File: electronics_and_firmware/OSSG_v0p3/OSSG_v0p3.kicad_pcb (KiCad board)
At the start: 4 copper layers, 85 x 9 mm, 64 parts, among them IC1 DW01A, J1 USB_B_Micro, Q1 FS8205A, Q2 Q_NPN_BEC, Q3 Q_NPN_BEC, SW1 SW_SPST, U1 ESP32-PICO-D4, U2 TP4056, U3 XC6222B331MRG, U4 FT232RQ

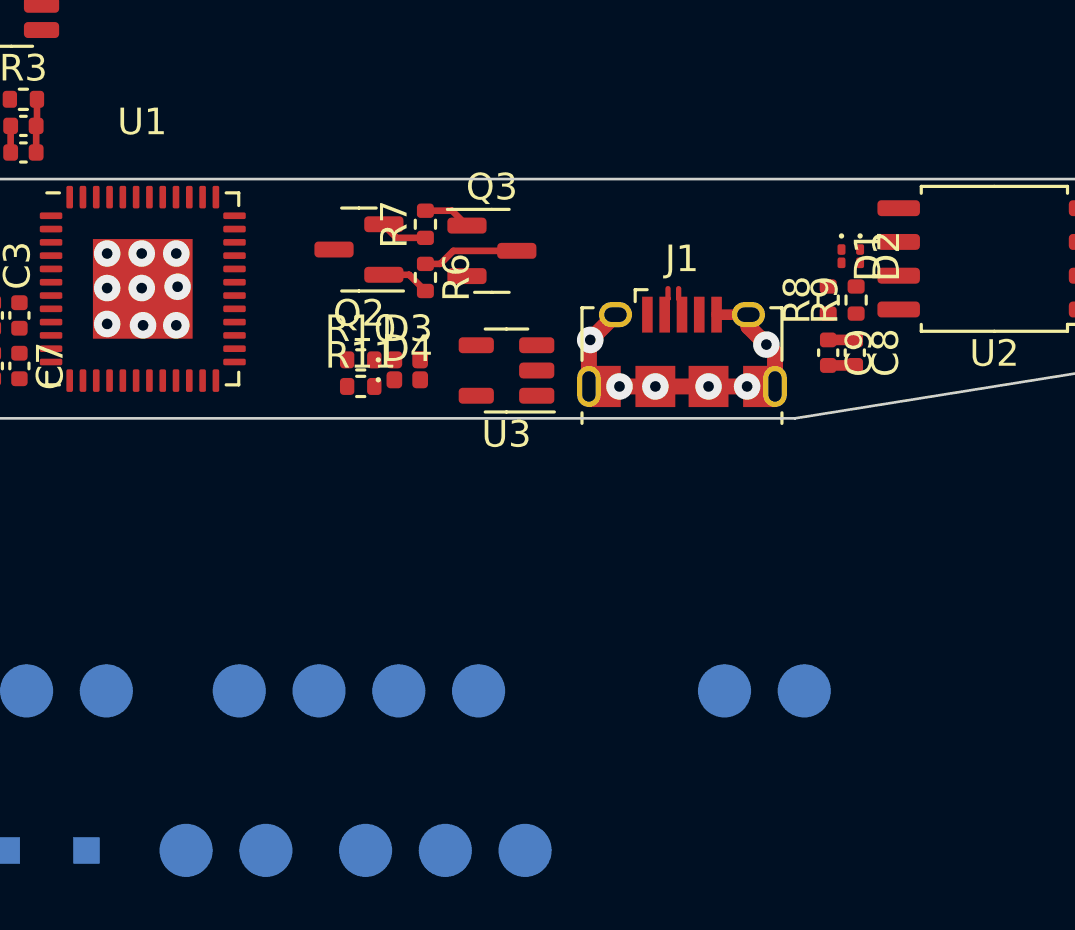
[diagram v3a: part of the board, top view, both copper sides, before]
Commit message: fix TX/RX switch, fix DW01A transistor symbol, update footprint sizes, remove IO0 and GPIOs at north side of ESP32-PICO-D4
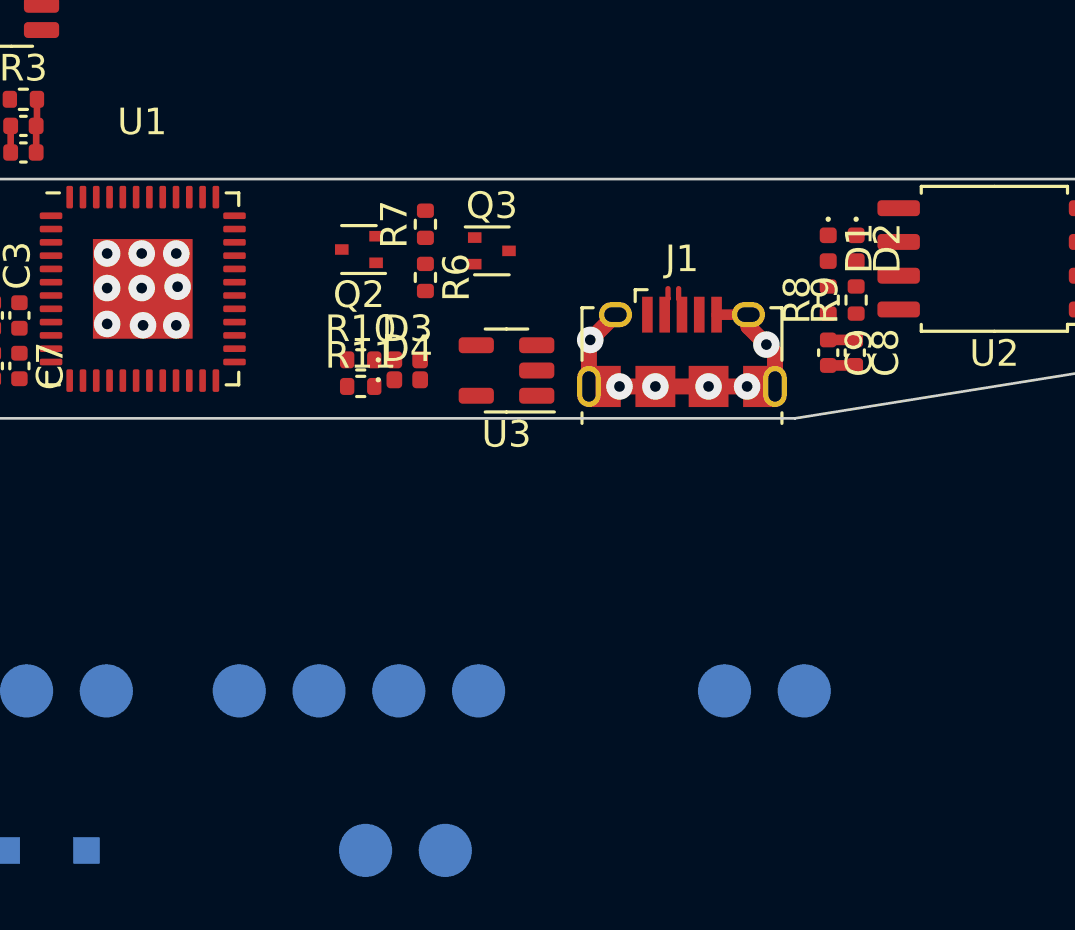
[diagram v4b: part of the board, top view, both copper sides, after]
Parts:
- removed TP23: IO0_Breakout, OpenSourceSmartGlasses:BreakoutPadSmall
- removed TP8: IO21_I2C_SDA0, OpenSourceSmartGlasses:BreakoutPadSmall
- removed TP9: IO22_I2C_SCL0, OpenSourceSmartGlasses:BreakoutPadSmall
- D1, D2: footprint Diode_SMD:D_01005_0402Metric -> Diode_SMD:D_0402_1005Metric
- Q2, Q3: footprint Package_TO_SOT_SMD:SOT-23 -> Package_TO_SOT_SMD:SOT-523
- moved D1 0.58 mm to (136.2, 77.6)
- moved D2 0.34 mm to (137.3, 77.6)
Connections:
- Q1 pad 1: Net-(Q1-Pad1) -> GND
- Q1 pad 2: BATT- -> unconnected-(Q1-Pad2)
- Q1 pad 5: Net-(IC1-Pad3) -> unconnected-(Q1-Pad5)
- Q1 pad 6: GND -> Net-(IC1-Pad3)
- TP3 pad 1: RXD -> TX_ESP
- TP4 pad 1: TXD -> RX_ESP
- U1 pad 40: RXD -> RX_ESP
- U1 pad 41: TXD -> TX_ESP
- U4 pad 2: RXD -> TX_ESP
- U4 pad 30: TXD -> RX_ESP
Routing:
- net DTR: track 3.64 -> 0.00 mm
- net Net-(Q2-Pad1): track 1.82 -> 0.00 mm
- net RTS: track 1.80 -> 0.00 mm
- net Net-(Q3-Pad1): track 1.79 -> 0.00 mm

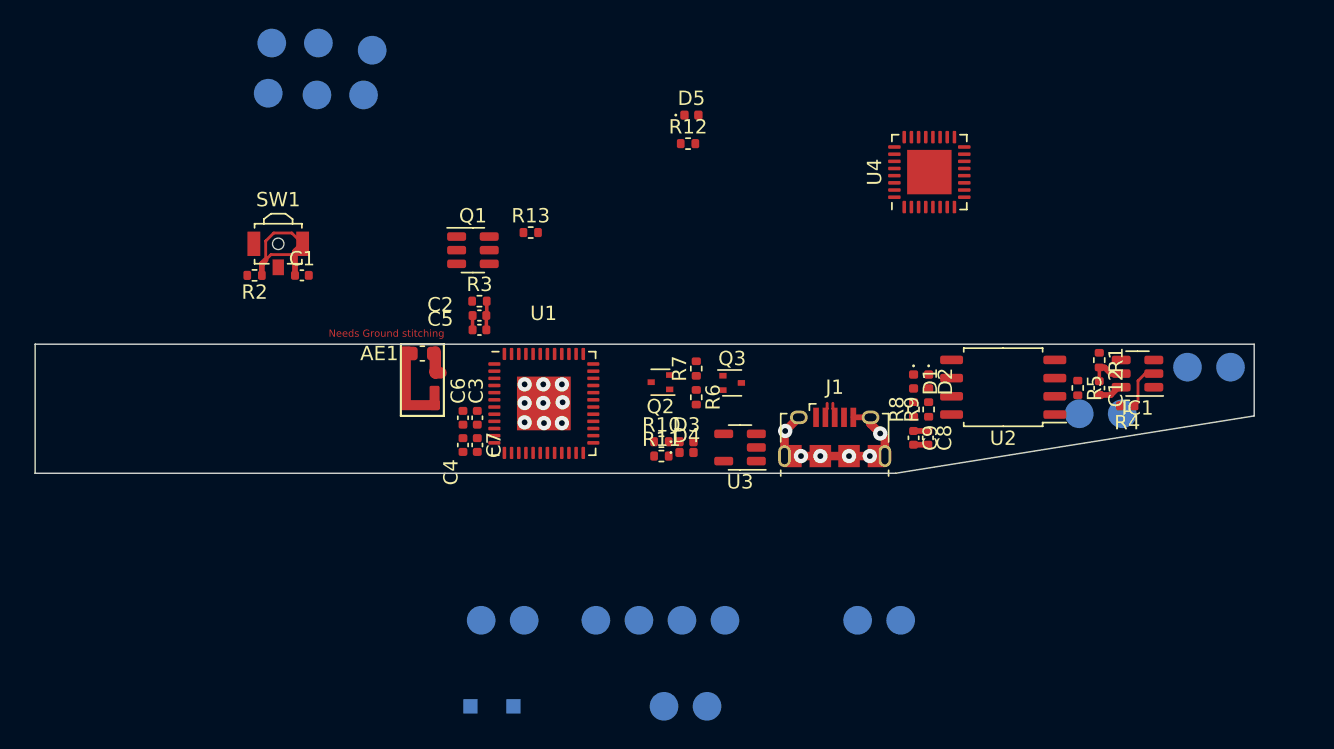
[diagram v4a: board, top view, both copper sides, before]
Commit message: more work on layout, small schematic fixes
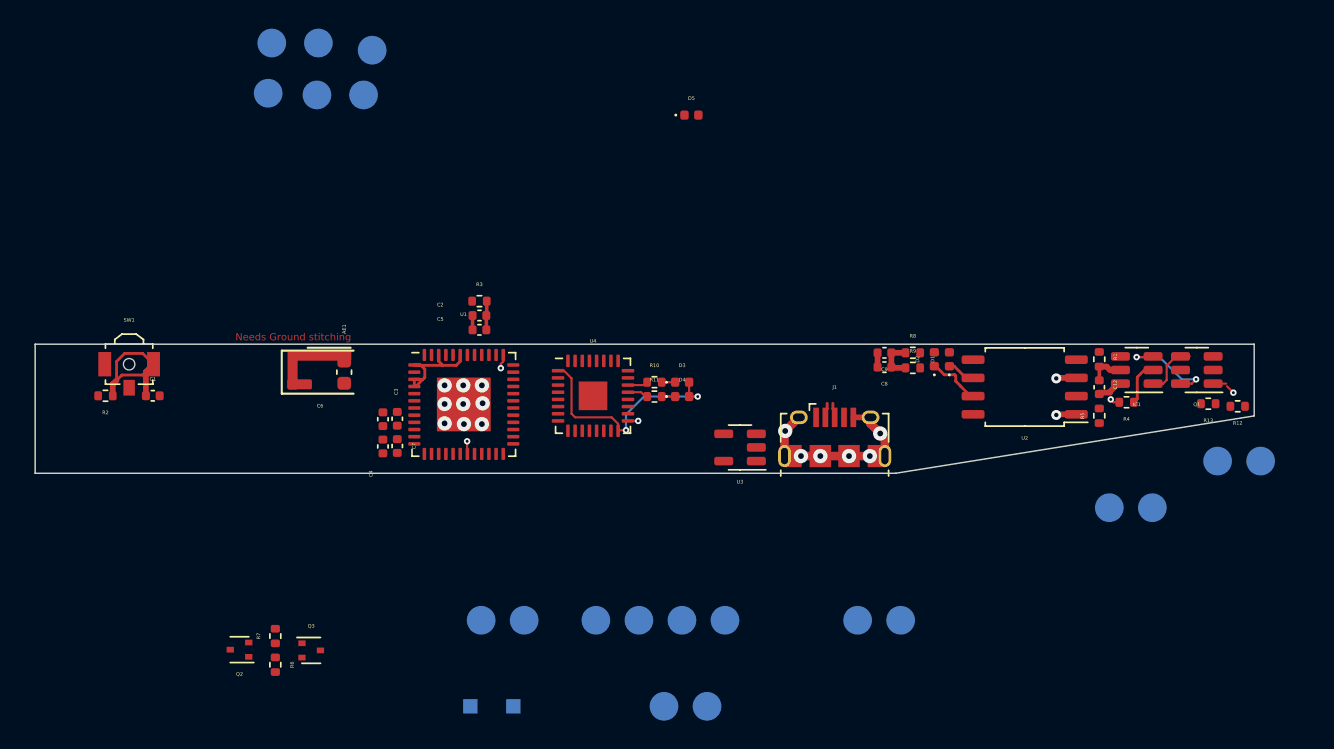
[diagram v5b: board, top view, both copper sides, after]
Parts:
- moved Q1 51.2 mm to (156.0, 76.8), turned to 180 degrees
- moved R13 48.7 mm to (156.8, 79.2), turned to 180 degrees
- moved R12 42.5 mm to (158.8, 79.3), turned to 180 degrees
- moved Q2 34.8 mm to (89.2, 96.3)
- moved Q3 34.8 mm to (94.2, 96.3)
- moved R6 34.8 mm to (91.8, 97.3)
- moved R7 34.8 mm to (91.8, 95.3)
- moved U4 28.2 mm to (113.9, 78.6), turned to 0 degrees
- moved SW1 13.4 mm to (81.6, 77.2)
- moved C1 13.4 mm to (83.2, 78.6)
- moved R2 13.4 mm to (79.9, 78.6)
- moved TP13 6.88 mm to (157.4, 83.2)
- moved TP14 6.88 mm to (149.9, 86.4)
- moved TP15 6.88 mm to (160.4, 83.2)
- moved TP16 6.88 mm to (152.9, 86.4)
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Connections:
- U1 pad 19: +3.3VA -> +3V3
- U1 pad 37: +3.3VA -> +3V3
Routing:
- net VCCIO: track 0.00 -> 16.4 mm, vias 0 -> 2
- net +3.3VA: track 2.01 -> 10.1 mm
- net Net-(IC1-Pad3): track 0.00 -> 7.17 mm, vias 0 -> 2
- net GND: track 15.5 -> 20.6 mm, vias 15 -> 20
- net Net-(D2-Pad1): track 0.00 -> 3.79 mm
- net Net-(IC1-Pad1): track 0.00 -> 3.60 mm
- net VCC_IN: track 1.06 -> 3.06 mm
- net Net-(D1-Pad1): track 0.00 -> 1.99 mm
- net +3V3: track 0.00 -> 1.88 mm, vias 0 -> 2
- net Net-(AE1-Pad1): track 1.86 -> 0.00 mm
- net Net-(R11-Pad1): track 0.00 -> 1.46 mm
- net Net-(R10-Pad1): track 0.00 -> 1.42 mm
- net Net-(D4-Pad1): track 0.00 -> 0.94 mm
- net Net-(D3-Pad1): track 0.00 -> 0.94 mm

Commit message: Changed antenna and routing progress
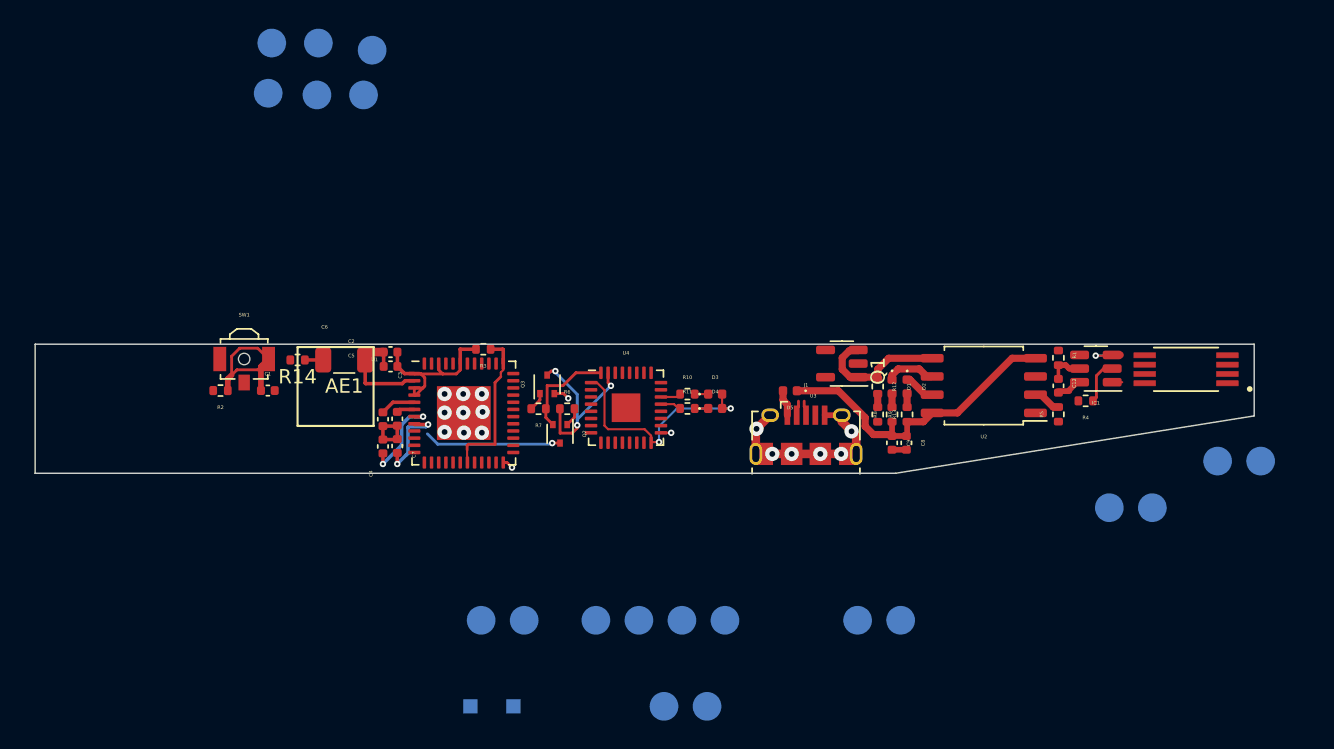
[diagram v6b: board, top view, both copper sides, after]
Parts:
- added R14: NC, Resistor_SMD:R_0402_1005Metric, F.Cu at (93.3, 76.1)
- AE1: value 2450AT14A0100T -> H2U34W1H1Z0400; footprint Capacitor_SMD:C_0603_1608Metric -> Resistor_SMD:R_1206_3216Metric
- Q1: footprint Package_TO_SOT_SMD:SOT-23-6 -> ESPGLASSES:SOP65P640X120-8N
- moved R6 27.1 mm to (112.1, 79.5), turned to 0 degrees
- moved Q2 26.9 mm to (111.6, 81.2), turned to -90 degrees
- moved R12 25.1 mm to (133.8, 78.0), turned to -90 degrees
- moved Q3 24.8 mm to (110.7, 77.8), turned to 90 degrees
- moved R7 24.2 mm to (110.1, 79.5), turned to 180 degrees
- moved R13 23.1 mm to (133.8, 79.9), turned to -90 degrees
- moved D5 20.4 mm to (127.6, 78.2), turned to 180 degrees
- moved U3 9.20 mm to (131.2, 76.3)
- moved C1 8.03 mm to (91.2, 78.2)
- moved R2 8.03 mm to (87.9, 78.2)
- moved SW1 8.03 mm to (89.6, 76.9)
- moved C2 6.70 mm to (99.8, 75.5)
- moved C5 6.70 mm to (99.8, 76.5)
- moved C9 6.30 mm to (134.8, 81.9), turned to -90 degrees
- moved C8 5.50 mm to (135.8, 81.9), turned to -90 degrees
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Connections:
- AE1 pad 2: (no net) -> Net-(AE1-Pad2)
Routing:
- net VCC_IN: track 3.06 -> 22.1 mm
- net DTR: track 0.00 -> 12.9 mm, vias 0 -> 3
- net EN: track 10.3 -> 20.0 mm, vias 0 -> 1
- net BATT+: track 0.00 -> 9.69 mm
- net +3V3: track 1.88 -> 10.9 mm, vias 2 -> 0
- net RTS: track 0.00 -> 7.08 mm
- net ADC1C1: track 0.00 -> 6.36 mm, vias 0 -> 2
- net ADC1C3: track 0.00 -> 6.09 mm, vias 0 -> 2
- net Net-(U1-Pad2): track 0.00 -> 5.06 mm
- net Net-(IC1-Pad3): track 7.17 -> 3.33 mm, vias 2 -> 1
- net Net-(IC1-Pad1): track 3.60 -> 0.70 mm
- net +3.3VA: track 10.1 -> 12.7 mm
- net ADC1C2: track 0.21 -> 2.69 mm
- net Net-(D1-Pad1): track 1.99 -> 4.01 mm
- net Net-(R5-Pad2): track 0.00 -> 1.96 mm
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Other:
- board text removed: "Needs Ground stitching"

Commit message: Routing progress and trial copper fill
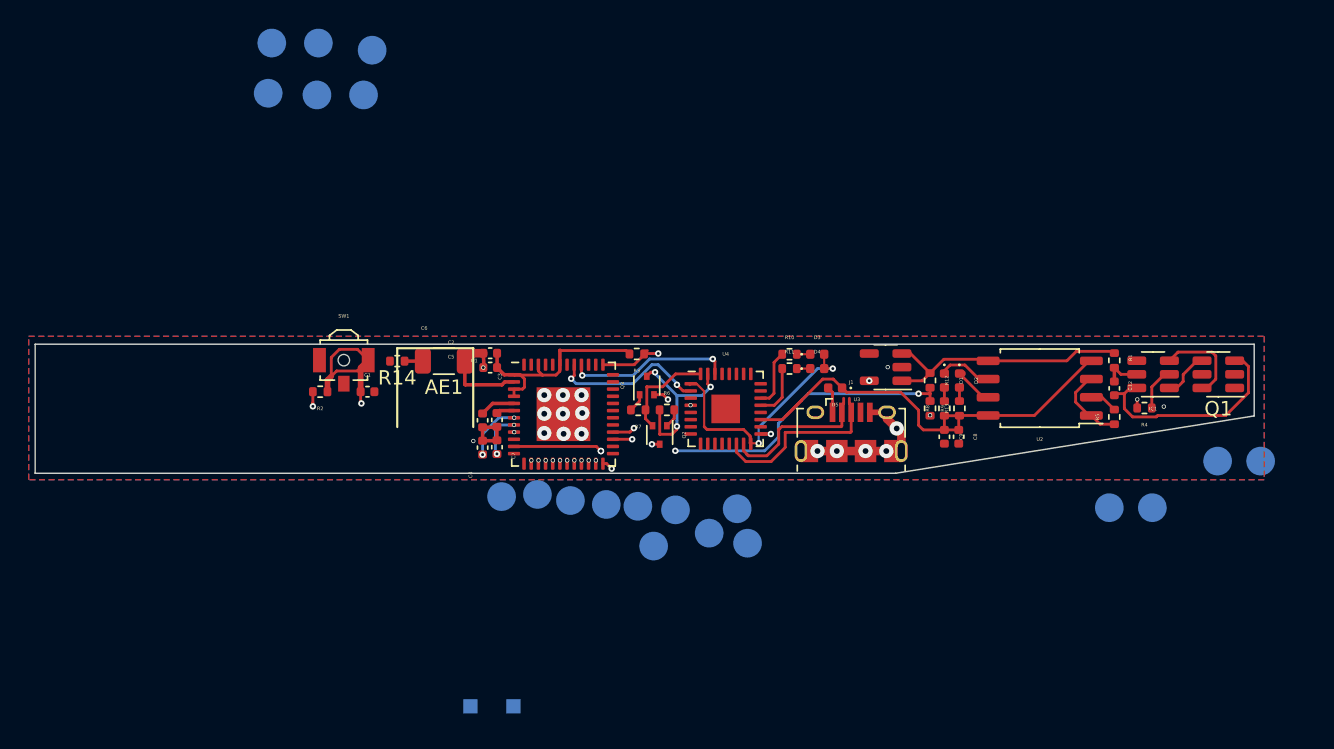
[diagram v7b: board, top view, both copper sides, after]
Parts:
- Q1: footprint ESPGLASSES:SOP65P640X120-8N -> Package_TO_SOT_SMD:SOT-23-6
- moved TP5 13.9 mm to (119.7, 86.5)
- moved TP25 13.8 mm to (124.0, 86.5)
- moved TP1 12.5 mm to (122.0, 88.2)
- moved TP22 11.6 mm to (114.8, 86.2)
- moved R3 10.7 mm to (117.0, 75.7)
- moved TP20 9.62 mm to (112.3, 85.9)
- moved TP24 9.37 mm to (124.7, 88.9)
- moved TP7 8.82 mm to (110.0, 85.5)
- moved TP6 8.74 mm to (107.5, 85.6)
- moved TP21 8.52 mm to (117.0, 86.3)
- moved D3 7.64 mm to (129.5, 75.7)
- moved D4 7.64 mm to (129.5, 76.7)
- moved R10 7.64 mm to (127.6, 75.7)
- moved R11 7.64 mm to (127.6, 76.7)
- moved AE1 6.95 mm to (103.5, 76.2)
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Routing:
- net IO35: track 0.93 -> 34.1 mm, vias 0 -> 4
- net EN: track 20.0 -> 35.6 mm, vias 1 -> 3
- net BATT-: track 1.75 -> 15.4 mm
- net Net-(J1-Pad3): track 1.03 -> 12.7 mm
- net RX_ESP: track 0.00 -> 11.4 mm, vias 0 -> 2
- net TX_ESP: track 0.00 -> 10.9 mm, vias 0 -> 2
- net VCC_IN: track 22.1 -> 32.6 mm
- net Net-(J1-Pad2): track 1.03 -> 11.0 mm
- net BATT+: track 9.69 -> 17.9 mm
- net IO0: track 1.15 -> 8.73 mm, vias 1 -> 2
- net +3.3VA: track 12.7 -> 15.8 mm
- net +3V3: track 10.9 -> 7.77 mm, vias 0 -> 4
- net Net-(IC1-Pad3): track 3.33 -> 6.43 mm, vias 1 -> 0
- net Net-(R10-Pad1): track 1.42 -> 4.32 mm
- net ADC1C3: track 6.09 -> 3.22 mm
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- added copper zone on B.Cu, net GND
- added copper zone on F.Cu, net GND

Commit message: lots of layout, fix footprint not found error, work towards better RF for antenna
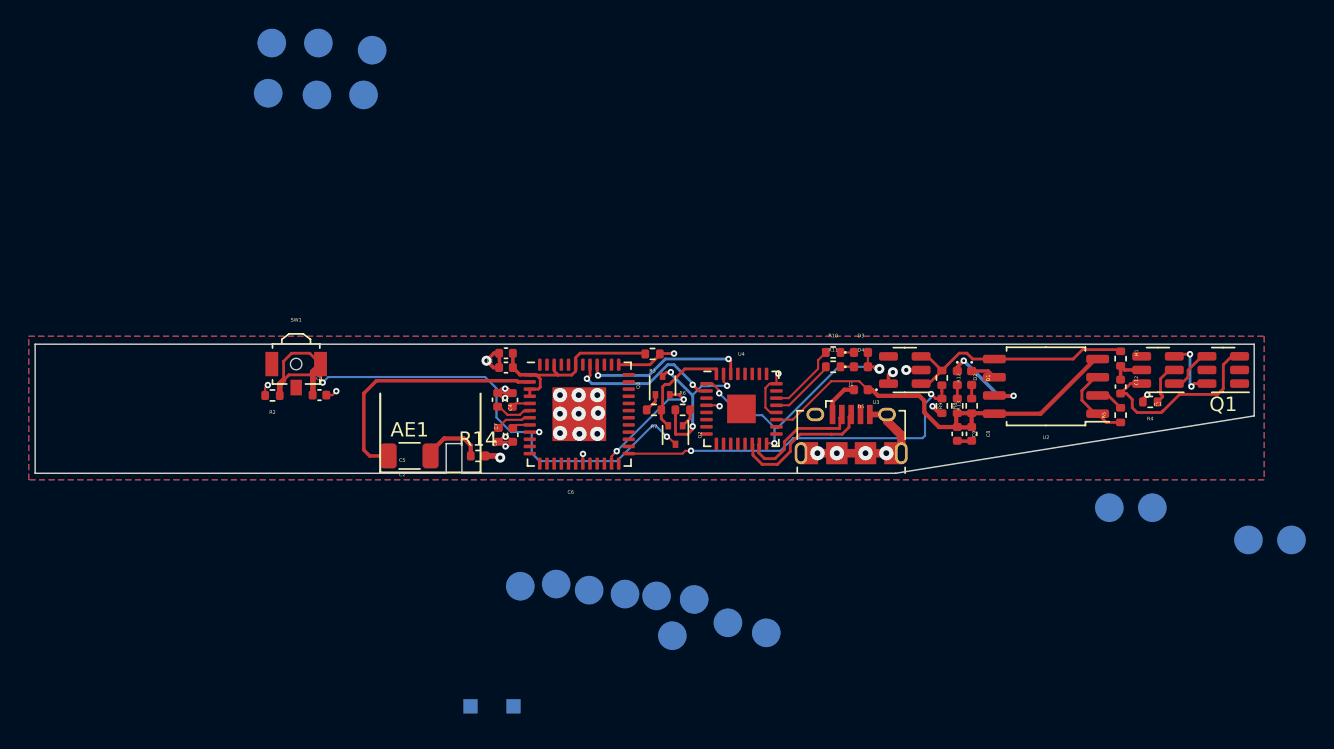
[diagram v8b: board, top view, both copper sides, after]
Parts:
- removed TP25: IO16_U2RXD, OpenSourceSmartGlasses:BreakoutPadSmall
- moved R14 8.69 mm to (105.9, 82.8), turned to 0 degrees
- moved AE1 7.03 mm to (101.1, 82.8), turned to 0 degrees
- moved TP1 6.38 mm to (123.3, 94.4)
- moved TP19 6.38 mm to (119.4, 95.3)
- moved TP24 6.38 mm to (126.0, 95.1)
- moved TP20 6.38 mm to (113.6, 92.2)
- moved TP21 6.38 mm to (118.3, 92.5)
- moved TP22 6.38 mm to (116.1, 92.4)
- moved TP5 6.38 mm to (121.0, 92.8)
- moved TP6 6.38 mm to (108.8, 91.9)
- moved TP7 6.38 mm to (111.3, 91.7)
- moved TP13 5.91 mm to (159.6, 88.7)
- moved TP15 5.91 mm to (162.6, 88.7)
- moved C1 3.36 mm to (94.8, 78.5)
- moved SW1 3.34 mm to (93.2, 77.2)
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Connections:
- net Net-(J1-Pad2) renamed USB-
- net Net-(J1-Pad3) renamed USB+
- R12 pad 2: IO35 -> IO16
- R13 pad 1: IO35 -> IO16
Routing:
- net IO35: track 34.1 -> 0.00 mm, vias 4 -> 0
- net IO16: track 0.00 -> 26.1 mm, vias 0 -> 2
- net GND: track 22.1 -> 36.9 mm, vias 22 -> 25
- net Net-(AE1-Pad1): track 5.06 -> 18.0 mm
- net EN: track 35.6 -> 44.1 mm
- net Net-(D2-Pad1): track 3.48 -> 7.60 mm, vias 0 -> 2
- net Net-(AE1-Pad2): track 1.28 -> 4.40 mm
- net USB+: track 12.7 -> 10.1 mm
- net VCC_IN: track 32.6 -> 30.1 mm
- net USB-: track 11.0 -> 8.68 mm
- net ADC1C3: track 3.22 -> 1.28 mm, vias 2 -> 0
- net ADC1C1: track 4.11 -> 2.51 mm, vias 2 -> 0
- net IO9: track 1.58 -> 0.00 mm, vias 1 -> 0
- net Net-(IC1-Pad3): track 6.43 -> 4.96 mm, vias 0 -> 2
- net Net-(D1-Pad1): track 4.19 -> 2.79 mm
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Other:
- outline, holes or cut-outs redrawn
- board text added: "Thermal Zone"
